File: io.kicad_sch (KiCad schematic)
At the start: 53 parts, among them J4 LASER, J6 TT143AMC12C, Q1 BSS214NW, U1 LSM6DSOXTR, U10 MAX30102, U11 TPS65631W, U12 TXB0102YZP, U14 LIS3MDL, U16 DRV2605LDGS, U7 LPS22DF, U8 TCA9406DC

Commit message: done with stm, going back to esp
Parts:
- added C19: 10uF, symbol Device:C_Small
- added C20: 100nF, symbol Device:C_Small
- added J3: Micro_SD_Card, Connector_Card:microSD_HC_Molex_104031-0811, symbol Connector:Micro_SD_Card
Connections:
- net +1V8: now also C19.1, C20.1, J3.4 (VDD)
- net GND: now also C19.2, C20.2, J3.6 (VSS), J3.9 (SHIELD)
- new net SD_CLK: J3.5 (CLK)
- new net SD_CMD: J3.3 (CMD)
- new net SD_D0: J3.7 (DAT0)
- new net SD_D1: J3.8 (DAT1)
- new net SD_D2: J3.1 (DAT2)
- new net SD_D3: J3.2 (DAT3/CD)
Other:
- moved on the sheet: C102, C104, C26, C27, C28, C32, C33, C35, C36, C38, C39, C40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

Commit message: quicksaving pcb bc im gonna redo it
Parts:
- removed C19: 10uF, symbol Device:C_Small
- removed C36, C38, C39, C40: 100nF, symbol Device:C_Small
- removed R22: 10k, symbol Device:R
- removed U12: TXB0102YZP, Package_BGA:Texas_DSBGA-8_0.9x1.9mm_Layout2x4_P0.5mm, symbol Logic_LevelTranslator:TXB0102YZP
- removed U8: TCA9406DC, symbol Interface:TCA9406DC
- added C91: 10uF, Capacitor_SMD:C_0402_1005Metric, symbol Device:C_Small
- added D16, D17, D18, D19, D20, D21, D22: ESD9B3.3ST5G, Diode_SMD:D_SOD-923, symbol Diode:ESD9B3.3ST5G
- added R10: 10k, symbol Device:R
- added R58, R59, R63, R64, R65, R66: 10k, Resistor_SMD:R_0402_1005Metric, symbol Device:R
- added R9: 0, symbol Device:R
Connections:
- net +1V8: no longer C20.1, C26.1, C35.1, C66.1, C67.2, C68.2, C69.2, C72.2, C74.2, J3.4 (VDD), MK1.5 (VDD), MK2.5 (VDD), U1.12 (CS), U1.5 (VDDIO), U1.8 (VDD), U14.10 (~{CS}), U14.6 (Vdd_IO), U7.1 (Vdd_IO)
- net +3V3: now also C20.2, C26.1, C35.1, C66.1, C67.2, C68.2, C69.2, C72.2, C74.2, J3.4 (VDD), MK1.5 (VDD), MK2.5 (VDD), U1.12 (CS), U1.5 (VDDIO), U1.8 (VDD), U14.10 (~{CS}), U14.6 (Vdd_IO), U7.1 (Vdd_IO), C91.2, D22.2 (A2), R10.1, R58.1, R59.1, R63.1, R64.1, R65.1, R66.1
- net GND: now also C104.2, C20.1, C91.1, D16.1 (A1), D17.1 (A1), D18.1 (A1), D19.1 (A1), D20.1 (A1), D21.1 (A1), D22.1 (A1), R9.1; no longer C104.1, C20.2, J6.24 (MTP_PWR)
- net HBT_INT: now also R10.2
- net SD_CLK: now also D19.2 (A2), R64.2
- net SD_CMD: now also D18.2 (A2), R63.2
- net SD_D0: now also D20.2 (A2), R65.2
- net SD_D1: now also D21.2 (A2), R66.2
- net SD_D2: now also D16.2 (A2), R58.2
- net SD_D3: now also D17.2 (A2), R59.2
- net TP_INT: now also J6.2 (INT)
- net TP_RST: now also J6.5 (RST)
- net at U16.1 (REG): now also C104.1; no longer C104.2
- net TP_SDA: now reaches J6.3 (SDA)
- net TP_SCL: now reaches J6.4 (SCL)
- net SCL1 renamed IMU_SCL
- removed net SCL2: U10.2 (SCL), U14.1 (SCL/SPC), U16.2 (SCL), U7.2 (SCL)
- net SDA1 renamed IMU_SDA
- removed net SDA2: U10.3 (SDA), U14.11 (SDA/SDI/SDO), U16.3 (SDA), U7.4 (SDA)
- new net: J6.24 (MTP_PWR), R9.2
- new net ALT_SCL: U7.2 (SCL)
- new net ALT_SDA: U7.4 (SDA)
- new net HBT_SCL: U10.2 (SCL)
- new net HBT_SDA: U10.3 (SDA)
- new net MAG_SCL: U14.1 (SCL/SPC)
- new net MAG_SDA: U14.11 (SDA/SDI/SDO)
- new net MTR_SCL: U16.2 (SCL)
- new net MTR_SDA: U16.3 (SDA)
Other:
- note removed: "internal 10k pull-ups, check these later"
- moved on the sheet: C102, C104, C20, C32, C33, C35, C54, C55, C56, C57, C58, C64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

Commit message: no more daughter probably
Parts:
- removed C51: 100nF, symbol Device:C_Small
- removed C53: 10uF, symbol Device:C_Small
- removed C72: 100nF, Capacitor_SMD:C_0402_1005Metric, symbol Device:C_Small
- removed J4: LASER, symbol Connector:Conn_01x02_Socket
- removed Q1: BSS214NW, Package_TO_SOT_SMD:SOT-323_SC-70, symbol Transistor_FET:BSS214NW
- removed R20, R21: 10k, symbol Device:R
- added C81: 100nF, Capacitor_SMD:C_0402_1005Metric, symbol Device:C_Small
- added C82: 1uF, Capacitor_SMD:C_0402_1005Metric, symbol Device:C_Small
- added D16: LED, symbol Device:LED
- added D17: APFA3010, LED_SMD:LED_Kingbright_APFA3010_3x1.5mm_Horizontal, symbol LED:APFA3010
- added U16: LT3465, Package_TO_SOT_SMD:TSOT-23-6, symbol Driver_LED:LT3465
- added U17: KTD2026, Package_DFN_QFN:DFN-8-1EP_1.5x1.5mm_P0.4mm_EP0.7x1.2mm, symbol Driver_LED:KTD2026
- C49: renamed from C27; footprint (none) -> Capacitor_SMD:C_0603_1608Metric
- C53: renamed from C28; footprint (none) -> Capacitor_SMD:C_0402_1005Metric
- C54: renamed from C26; footprint (none) -> Capacitor_SMD:C_0402_1005Metric
- C61: renamed from C20; footprint (none) -> Capacitor_SMD:C_0402_1005Metric
- C73: renamed from C56; footprint Capacitor_SMD:C_0402_1005Metric -> Capacitor_SMD:C_0603_1608Metric
- R44: renamed from R9; footprint (none) -> Resistor_SMD:R_0402_1005Metric
- R46: renamed from R10; footprint (none) -> Resistor_SMD:R_0402_1005Metric
- renumbered C70 to C48, C71 to C50, C52 to C55, C50 to C56, C63 to C57, C62 to C58, C73 to C59, C91 to C60, C32 to C62, C64 to C63, C33 to C64, C58 to C65, C35 to C66, C68 to C67, C74 to C68, C67 to C69, C69 to C70, C65 to C71, C55 to C72, C66 to C74, C102 to C75, C54 to C76, C57 to C77, C104 to C78, D17 to D10, D18 to D11, D19 to D12, D20 to D13, D21 to D14, D22 to D15, D16 to D9, J3 to J5, L8 to L7, L7 to L8, R58 to R38, R59 to R39, R63 to R40, R64 to R41, R65 to R42, R66 to R43, R54 to R45, U14 to U10, U7 to U11, U1 to U12, U16 to U13, U10 to U14, U11 to U9
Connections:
- net +3V3: now also C81.2, C82.1, D17.2 (A), U17.5 (VIN)
- net GND: now also C81.1, C82.2, U17.8 (GND), U17.9 (GND)
- new net: D17.4 (B), U17.2 (D3)
- new net: D17.3 (G), U17.3 (D2)
- new net: D17.1 (R), U17.4 (D1)
- new net LED_SCL: U17.6 (SCL)
- new net LED_SDA: U17.7 (SDA)
- no-connect marks 2 -> 3
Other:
- moved on the sheet: C60, C61, C62, C63, C64, C65, C66, J6, R44

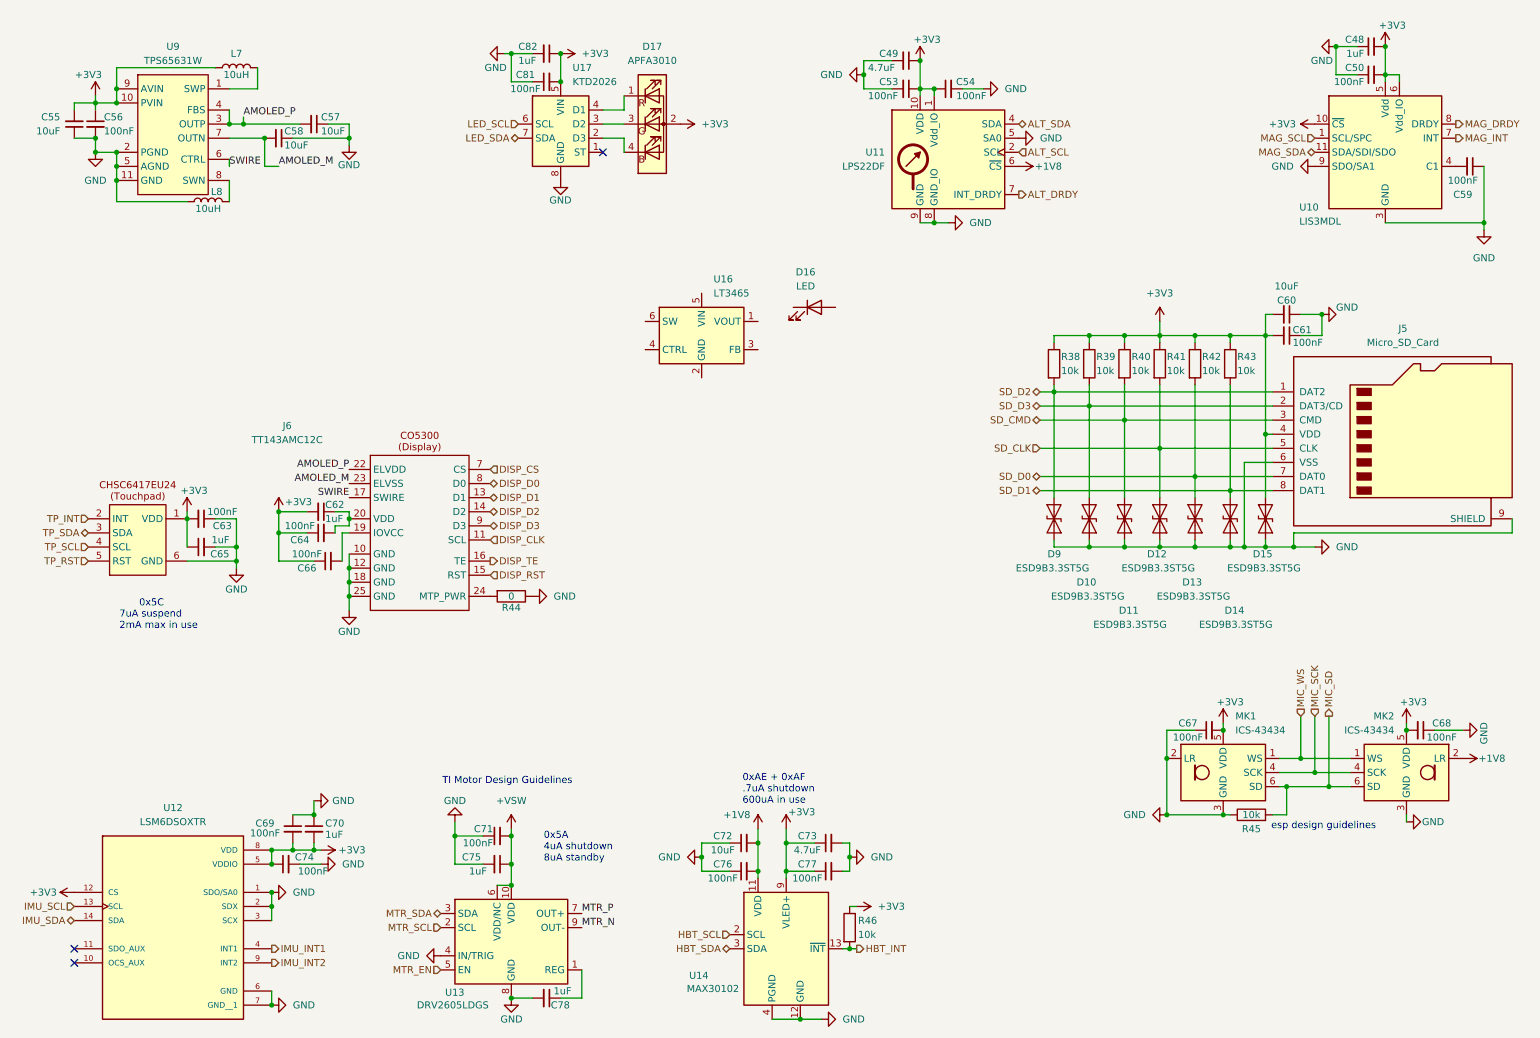
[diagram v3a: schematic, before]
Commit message: basically done with board layout, gonna try to do a smaller one (47->42mm diameter)
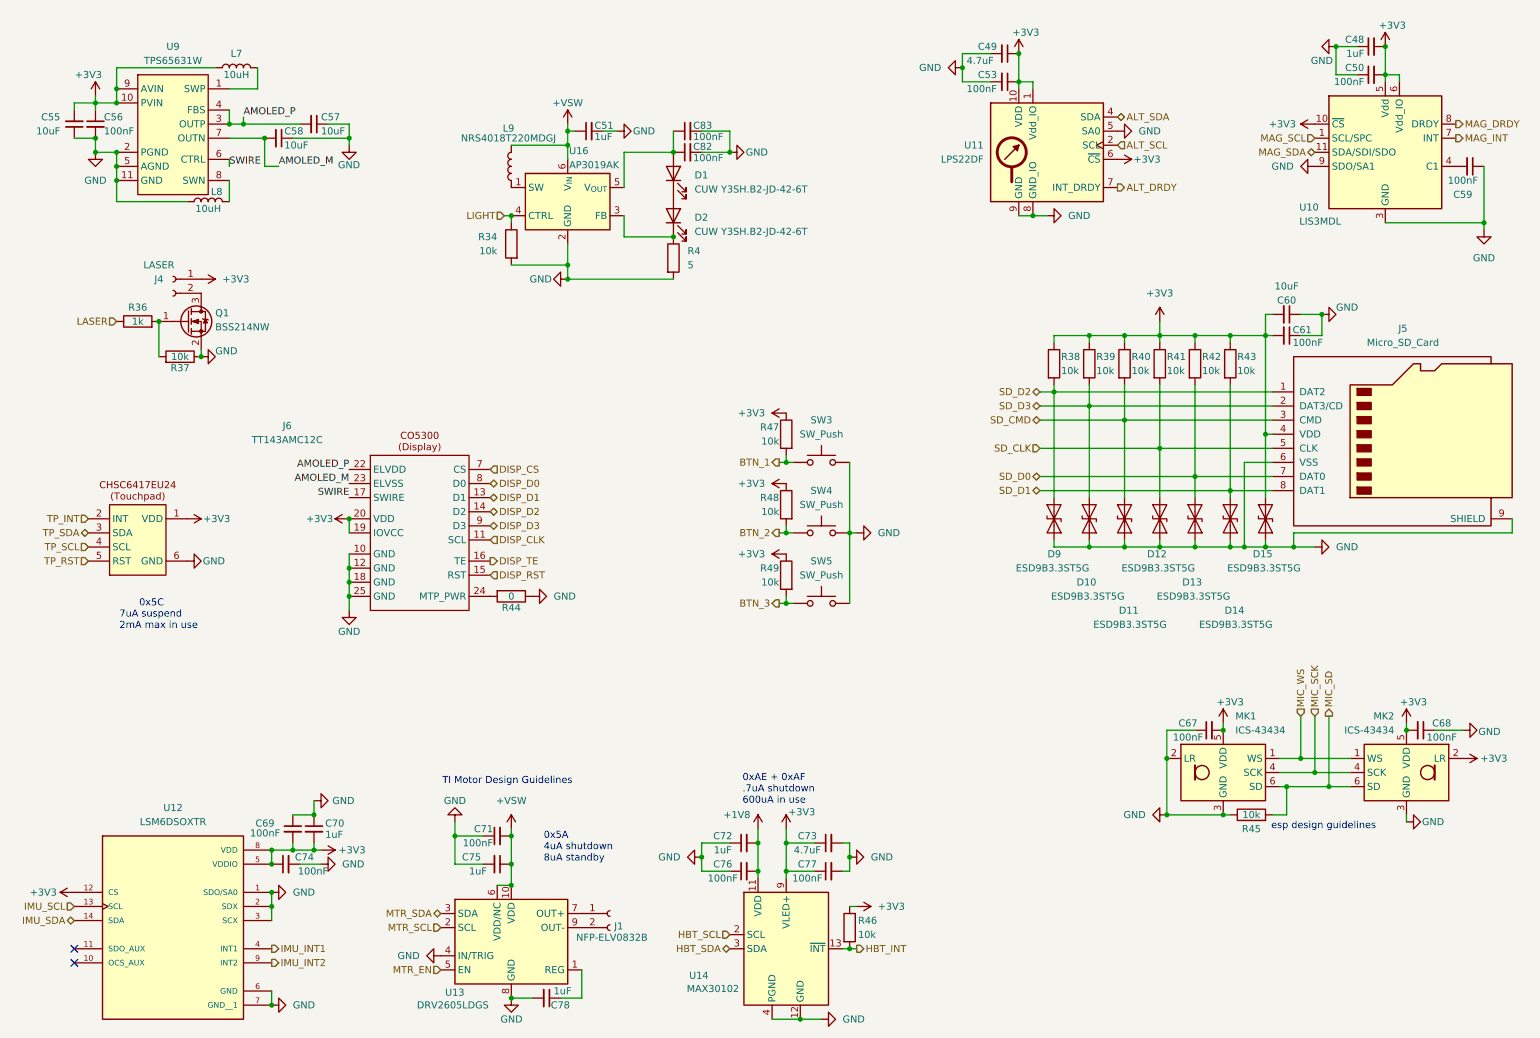
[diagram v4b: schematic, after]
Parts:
- removed C54, C63, C64, C66, C81: 100nF, Capacitor_SMD:C_0402_1005Metric, symbol Device:C_Small
- removed C62, C65: 1uF, Capacitor_SMD:C_0402_1005Metric, symbol Device:C_Small
- removed D16: LED, symbol Device:LED
- removed D17: APFA3010, LED_SMD:LED_Kingbright_APFA3010_3x1.5mm_Horizontal, symbol LED:APFA3010
- removed U16: LT3465, Package_TO_SOT_SMD:TSOT-23-6, symbol Driver_LED:LT3465
- removed U17: KTD2026, Package_DFN_QFN:DFN-8-1EP_1.5x1.5mm_P0.4mm_EP0.7x1.2mm, symbol Driver_LED:KTD2026
- added C51: 1uF, Capacitor_SMD:C_0402_1005Metric, symbol Device:C_Small
- added C83: 100nF, Capacitor_SMD:C_0402_1005Metric, symbol Device:C_Small
- added D1, D2: CUW Y3SH.B2-JD-42-6T, custom-lib:LED_CUW_Y3SH.B2-GFJD-5J6T-Z242-20-R18-Z, symbol Device:LED
- added J1: NFP-ELV0832B, custom-lib:Battery_Connector, symbol Connector:Conn_01x02_Socket
- added J4: LASER, custom-lib:LASER_connector, symbol Connector:Conn_01x02_Socket
- added L9: NRS4018T220MDGJ, Inductor_SMD:L_Taiyo-Yuden_MD-4040, symbol Device:L
- added Q1: BSS214NW, Package_TO_SOT_SMD:SOT-323_SC-70, symbol Transistor_FET:BSS214NW
- added R34, R47, R48, R49: 10k, Resistor_SMD:R_0402_1005Metric, symbol Device:R
- added R36: 1k, Capacitor_SMD:C_0402_1005Metric, symbol Device:R
- added R37: 10k, Capacitor_SMD:C_0402_1005Metric, symbol Device:R
- added R4: 5, Resistor_SMD:R_0402_1005Metric, symbol Device:R
- added SW3, SW4, SW5: SW_Push, Button_Switch_SMD:SW_SPST_B3U-3000P, symbol Switch:SW_Push
- added U16: AP3019AK, Package_TO_SOT_SMD:SOT-23-6, symbol Driver_LED:AP3019AKTR
- C72: value 10uF -> 1uF
- C82: value 1uF -> 100nF
- J5: footprint Connector_Card:microSD_HC_Molex_104031-0811 -> Connector_Card:microSD_HC_Hirose_DM3D-SF
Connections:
- net +1V8: no longer MK2.2 (LR), U11.6 (~{CS})
- net +3V3: now also J6.19 (IOVCC), J6.20 (VDD), MK2.2 (LR), U11.6 (~{CS}), J4.1 (Pin_1), R47.1, R48.1, R49.1; no longer C82.1
- net +VSW: now also C51.1, L9.2, U16.6 (V_{IN})
- net GND: now also C51.2, C83.2, Q1.2 (S), R34.2, R37.1, R4.2, SW3.2, SW4.2, SW5.2, U16.2 (GND)
- net MTR_N: no longer names the net of U13.9 (OUT-)
- net MTR_N: now also J1.2 (Pin_2)
- net MTR_P: no longer names the net of U13.7 (OUT+)
- net MTR_P: now also J1.1 (Pin_1)
- new net: L9.1, U16.1 (SW)
- new net: D2.1 (K), R4.1, U16.3 (FB)
- new net: C82.1, C83.1, D1.2 (A), U16.5 (V_{OUT})
- new net: Q1.1 (G), R36.2, R37.2
- new net: J4.2 (Pin_2), Q1.3 (D)
- new net: D1.1 (K), D2.2 (A)
- new net BTN_1: R47.2, SW3.1
- new net BTN_2: R48.2, SW4.1
- new net BTN_3: R49.2, SW5.1
- new net LASER: R36.1
- new net LIGHT: R34.1, U16.4 (CTRL)
- no-connect marks 3 -> 2
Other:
- moved on the sheet: C49, C53, U11

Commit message: layout done probably
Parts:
- removed R44: 0, Resistor_SMD:R_0402_1005Metric, symbol Device:R
- added C52: 1uF, Capacitor_SMD:C_0402_1005Metric, symbol Device:C_Small
- added R5: 10k, Resistor_SMD:R_0402_1005Metric, symbol Device:R
- added U15: APDS-9306-065, OptoDevice:Broadcom_DFN-6_2x2mm_P0.65mm, symbol Sensor_Optical:APDS-9306-065
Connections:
- net +3V3: now also C52.2, R5.2, U15.3 (VDD)
- net BTN_3: now also SW5.2; no longer SW5.1
- net GND: now also J6.24 (MTP_PWR), SW5.1, C52.1, U15.6 (GND); no longer SW5.2
- new net ALS_INT: R5.1, U15.4 (INT)
- new net ALS_SCL: U15.1 (SCL)
- new net ALS_SDA: U15.2 (SDA)
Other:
- note added: "1 and 24 should be towards the middle"
- moved on the sheet: C51, C82, C83, D1, D2, L9, R34, R4, R47, R48, R49, SW3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

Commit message: finally routed the memory :D
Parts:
- removed C49: 4.7uF, Capacitor_SMD:C_0603_1608Metric, symbol Device:C_Small
- removed C53, C83: 100nF, Capacitor_SMD:C_0402_1005Metric, symbol Device:C_Small
- removed J1: NFP-ELV0832B, custom-lib:Battery_Connector, symbol Connector:Conn_01x02_Socket
- removed J4: LASER, custom-lib:LASER_connector, symbol Connector:Conn_01x02_Socket
- removed R34: 10k, Resistor_SMD:R_0402_1005Metric, symbol Device:R
- removed R37: 10k, Capacitor_SMD:C_0402_1005Metric, symbol Device:R
- removed SW5: SW_Push, Button_Switch_SMD:SW_SPST_B3U-3000P, symbol Switch:SW_Push
- removed U11: LPS22DF, Package_LGA:ST_HLGA-10_2x2mm_P0.5mm_LayoutBorder3x2y, symbol Sensor_Pressure:LPS22DF
- added C54, C62: 100nF, Capacitor_SMD:C_0402_1005Metric, symbol Device:C_Small
- added J10: LASER-, TestPoint:TestPoint_Keystone_5015_Micro_Mini, symbol Connector:Conn_01x01_Socket
- added J11: MTR+, TestPoint:TestPoint_THTPad_1.5x1.5mm_Drill0.7mm, symbol Connector:Conn_01x01_Socket
- added J13: MTR-, TestPoint:TestPoint_THTPad_1.5x1.5mm_Drill0.7mm, symbol Connector:Conn_01x01_Socket
- added unit 2 of J6
- added J9: LASER+, TestPoint:TestPoint_Keystone_5015_Micro_Mini, symbol Connector:Conn_01x01_Socket
- added SW2: B3U-3000P-B, Button_Switch_SMD:SW_SPST_B3U-3000P-B, symbol Switch:SW_Push
- added U3: BME280, Package_LGA:Bosch_LGA-8_2.5x2.5mm_P0.65mm_ClockwisePinNumbering, symbol Sensor:BME280
- C51: footprint Capacitor_SMD:C_0402_1005Metric -> Capacitor_SMD:C_0603_1608Metric
- C55, C57, C58: footprint Capacitor_SMD:C_0402_1005Metric -> Capacitor_SMD:C_0805_2012Metric
- C82: value 100nF -> 220nF; footprint Capacitor_SMD:C_0402_1005Metric -> Capacitor_SMD:C_0603_1608Metric
- J5: footprint Connector_Card:microSD_HC_Hirose_DM3D-SF -> custom-lib:MOLEX_503398-1892
- J6: footprint custom-lib:OK-14GF024-04 -> custom-lib:MOLEX_505550-2420
- L9: value NRS4018T220MDGJ -> LQM2HPN4R7MG0L; footprint Inductor_SMD:L_Taiyo-Yuden_MD-4040 -> Inductor_SMD:L_1008_2520Metric
- R4: footprint Resistor_SMD:R_0402_1005Metric -> Resistor_SMD:R_0603_1608Metric
- R45, R46, R47, R48, R49, R5: value 10k -> 100k
- SW3, SW4: value SW_Push -> B3U-3000P-B; footprint Button_Switch_SMD:SW_SPST_B3U-3000P -> Button_Switch_SMD:SW_SPST_B3U-3000P-B
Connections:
- net +3V3: now also C54.1, C62.1, J6.19 (IOVCC), J6.20 (VDD), J9.1 (Pin_1), U3.2 (CSB), U3.6 (VDDIO), U3.8 (VDD); no longer J6.19 (IOVCC), J6.20 (VDD)
- net AMOLED_M: now also J6.23 (ELVSS); no longer J6.23 (ELVSS)
- net AMOLED_P: now also J6.22 (ELVDD); no longer J6.22 (ELVDD)
- net BTN_1: now also SW2.1; no longer SW3.1
- net BTN_2: now also SW3.2; no longer SW4.1
- net BTN_3: now also SW4.1
- net DISP_CLK: now also J6.11 (SCL); no longer J6.11 (SCL)
- net DISP_CS: now also J6.7 (CS); no longer J6.7 (CS)
- net DISP_D0: now also J6.8 (D0); no longer J6.8 (D0)
- net DISP_D1: now also J6.13 (D1); no longer J6.13 (D1)
- net DISP_D2: now also J6.14 (D2); no longer J6.14 (D2)
- net DISP_D3: now also J6.9 (D3); no longer J6.9 (D3)
- net DISP_RST: now also J6.15 (RST); no longer J6.15 (RST)
- net DISP_TE: now also J6.16 (TE); no longer J6.16 (TE)
- net GND: now also SW3.1, C54.2, C62.2, J6.10 (GND), J6.12 (GND), J6.18 (GND), J6.24 (MTP_PWR), J6.SH (SHIELD), SW2.2, U3.1 (GND), U3.5 (SDO), U3.7 (GND); no longer J6.10 (GND), J6.12 (GND), J6.18 (GND), J6.24 (MTP_PWR), J6.25 (GND), SW3.2
- net SWIRE: now also J6.17 (SWIRE); no longer J6.17 (SWIRE)
- net at U13.7 (OUT+): now also J11.1 (Pin_1)
- net at U13.9 (OUT-): now also J13.1 (Pin_1)
- net at Q1.3 (D): now also J10.1 (Pin_1)
- new net TPH_SCL: U3.4 (SCK)
- new net TPH_SDA: U3.3 (SDI)
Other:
- note added: "100mA max"
- note added: "200mA max"
- note added: "20mA typ 100mA max (?)"
- note added: "40 mA max"
- note added: "https://docs.rs/bme280-rs/latest/bme280_rs/"
- moved on the sheet: C52, Q1, R36, R47, R48, R49, R5, U15
